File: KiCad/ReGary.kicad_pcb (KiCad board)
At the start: 4 copper layers, 38 x 38 mm, 38 parts, among them J1 Conn_01x02, U1 GW1N-UV1P5LQ100, U2 LM1117-3.3, U3 TPS73643DBV, U4 SN74CBT16210, U5 SN74CBT16210, U6 SN74CBT16210, U7 SN74CBT16210, U8 PLCC_84_plug, U9 PLCC_84_plug

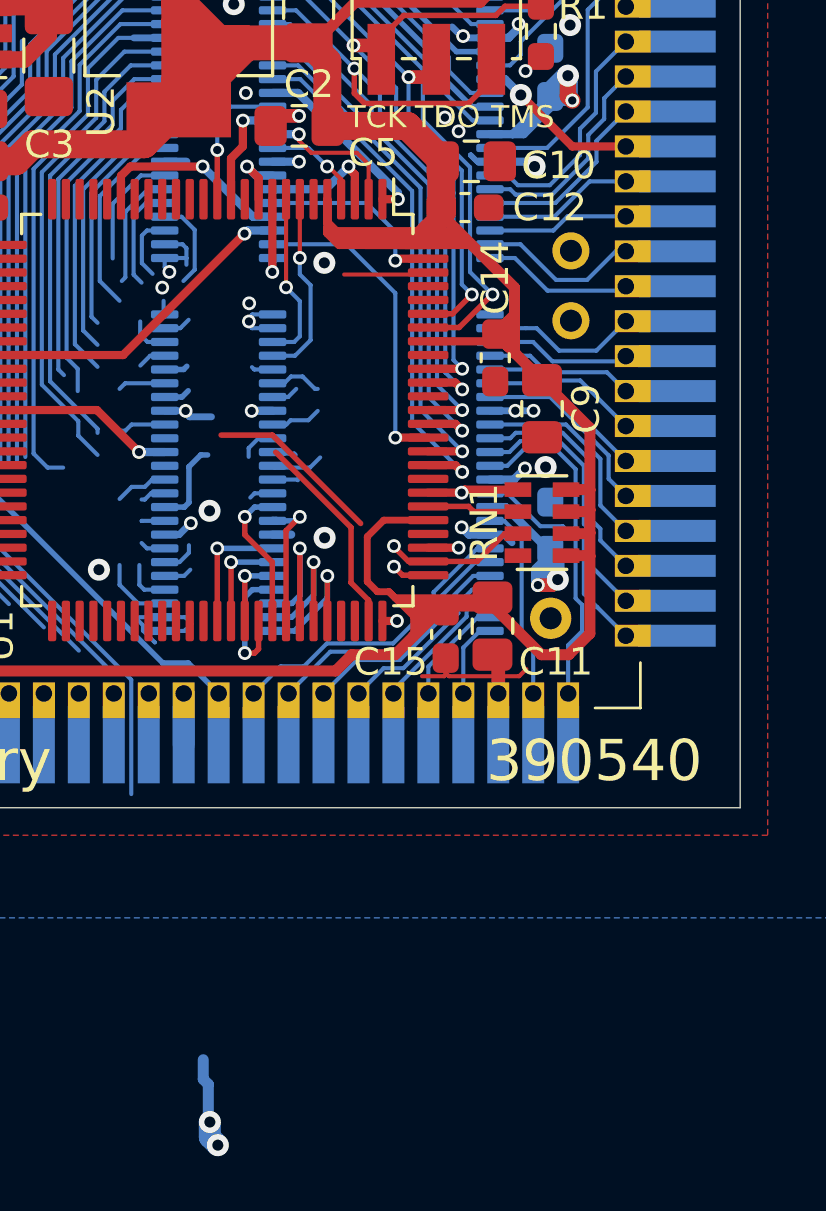
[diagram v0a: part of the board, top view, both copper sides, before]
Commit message: More signal to pin assignments and routing done, moved /REGEN and /RAMEN signals to FPGA pin 97,98
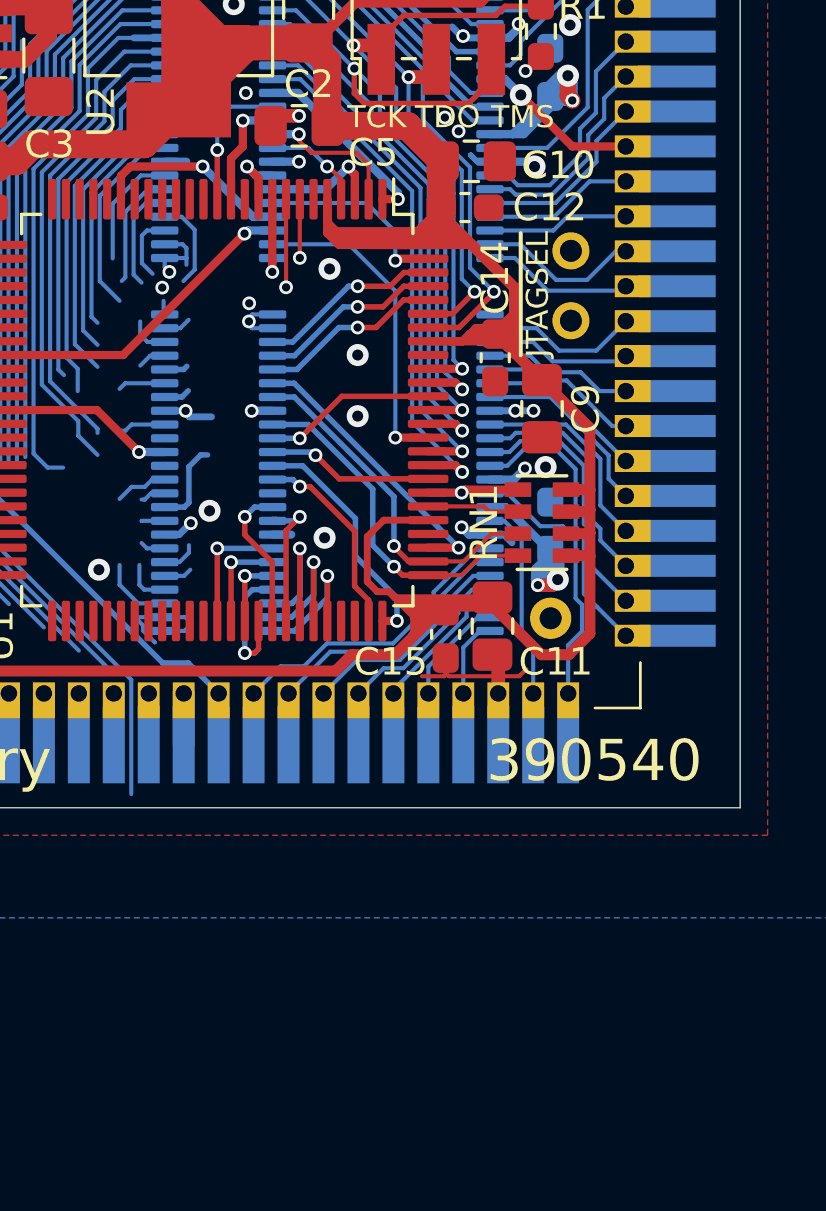
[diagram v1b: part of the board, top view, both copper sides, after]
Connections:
- U1 pad 7: REGEN_FPGA -> Net-(U1-Pad7)
- U1 pad 8: RAMEN_FPGA -> Net-(U1-Pad8)
- U1 pad 83: Net-(U1-Pad83) -> PWRUP_FPGA
- U1 pad 89: Net-(U1-Pad89) -> A12_FPGA
- U1 pad 96: Net-(U1-Pad96) -> BLS_FPGA
- U1 pad 97: Net-(U1-Pad97) -> REGEN_FPGA
- U1 pad 98: Net-(U1-Pad98) -> RAMEN_FPGA
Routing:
- net UDS_FPGA: track 3.22 -> 12.7 mm
- net DBR_FPGA: track 3.04 -> 10.3 mm
- net LDS_FPGA: track 6.16 -> 12.9 mm
- net BLS_FPGA: track 0.79 -> 6.70 mm, vias 0 -> 1
- net PWRUP_FPGA: track 0.88 -> 6.06 mm, vias 0 -> 1
- net A12_FPGA: track 1.34 -> 6.28 mm, vias 0 -> 1
- net Net-(U1-Pad8): track 0.00 -> 3.20 mm, vias 0 -> 1
- net Net-(U1-Pad98): track 3.08 -> 0.00 mm
- net Net-(U1-Pad7): track 0.00 -> 2.13 mm, vias 0 -> 1
- net OECD_FPGA: track 8.46 -> 7.23 mm, vias 0 -> 1
- net Net-(U6-Pad35): track 0.87 -> 0.00 mm
- net 3V3: track 156.4 -> 156.3 mm, vias 2 -> 0
- net GND: vias 37 -> 39
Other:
- board text added: "~JTAGSEL"

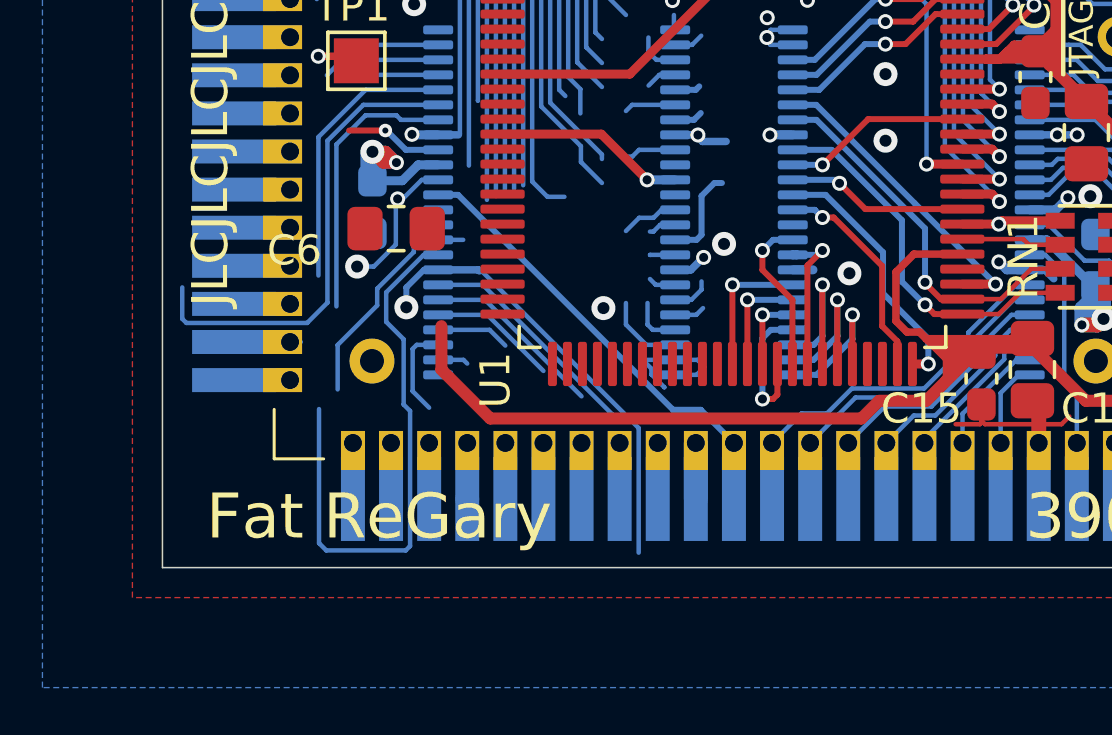
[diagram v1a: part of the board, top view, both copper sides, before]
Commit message: More pin assignments and routing
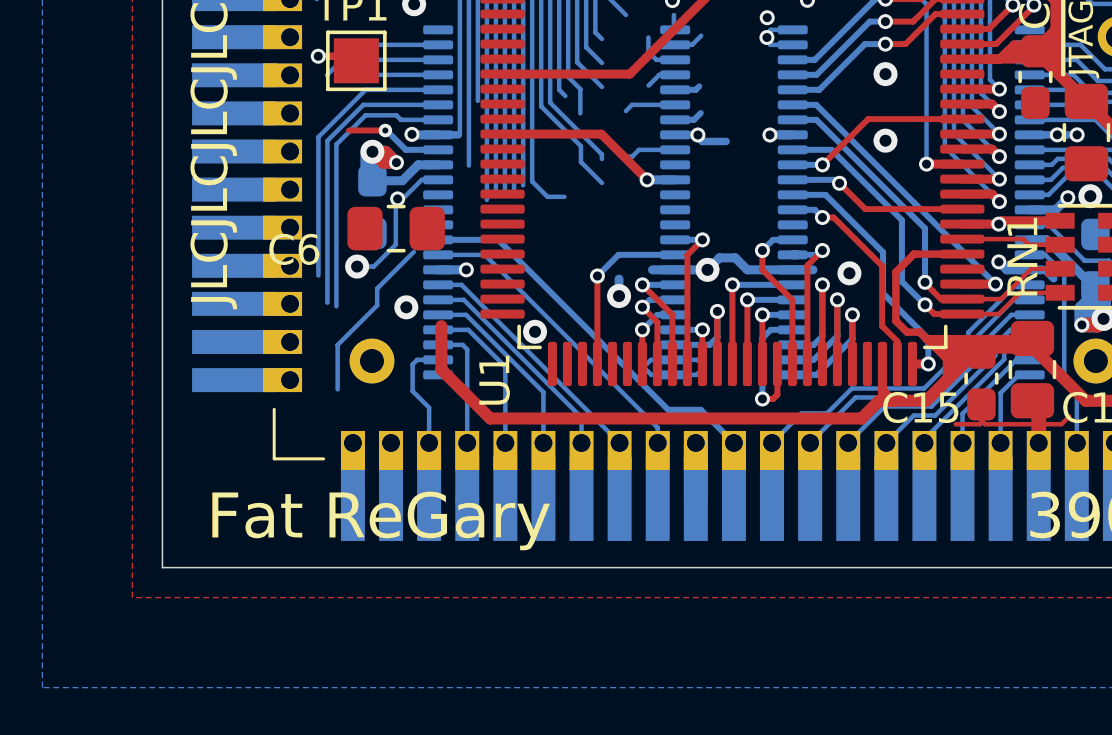
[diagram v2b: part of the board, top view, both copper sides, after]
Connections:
- net ABOE2 renamed Net-(U7-Pad11)
- net ABOE2_FPGA renamed Net-(U7-Pad37)
- net DBOE1 renamed Net-(U7-Pad12)
- net DBOE1_FPGA renamed Net-(U7-Pad36)
- net HLT renamed Net-(U7-Pad21)
- net HLT_FPGA renamed Net-(U7-Pad28)
- U1 pad 54: Net-(U1-Pad54) -> BERR_FPGA
- U1 pad 57: Net-(U1-Pad57) -> ROMJP0_FPGA
- U1 pad 58: Net-(U1-Pad58) -> ROMJP1_FPGA
- U1 pad 59: Net-(U1-Pad59) -> AVEC_FPGA
- U1 pad 60: Net-(U1-Pad60) -> CIIN_FPGA
- U1 pad 61: Net-(U1-Pad61) -> RESET_FPGA
- U1 pad 62: Net-(U1-Pad62) -> A15_FPGA
- U5 pad 42: CIIN_FPGA -> Net-(U5-Pad42)
- U5 pad 6: CIIN -> Net-(U5-Pad6)
- U7 pad 10: LOCK_EA1 -> CPUCLK
- U7 pad 13: CPUCLK -> Net-(U7-Pad13)
- U7 pad 14: GND -> Net-(U7-Pad14)
- U7 pad 16: BERR -> Net-(U7-Pad16)
- U7 pad 18: C7M -> Net-(U7-Pad18)
- U7 pad 19: RESET -> Net-(U7-Pad19)
- U7 pad 2: DBR16 -> A15
- U7 pad 20: CPUCLK -> Net-(U7-Pad20)
- U7 pad 3: DBOE0 -> RESET
- U7 pad 30: RESET_FPGA -> Net-(U7-Pad30)
- U7 pad 31: C7M_FPGA -> Net-(U7-Pad31)
- U7 pad 33: BERR_FPGA -> Net-(U7-Pad33)
- U7 pad 35: CPUCLK_FPGA -> Net-(U7-Pad35)
- U7 pad 38: LOCK_EA1_FPGA -> CPUCLK_FPGA
- U7 pad 39: CDAC_FPGA -> CIIN_FPGA
- U7 pad 4: DBLT -> ROMJP0
- U7 pad 40: EDS3_FPGA -> BERR_FPGA
- U7 pad 42: EDS2_FPGA -> AVEC_FPGA
- U7 pad 43: READ_FPGA -> ROMJP1_FPGA
- U7 pad 44: DBLT_FPGA -> ROMJP0_FPGA
- U7 pad 45: DBOE0_FPGA -> RESET_FPGA
- U7 pad 46: DBR16_FPGA -> A15_FPGA
- U7 pad 5: READ -> ROMJP1
- U7 pad 6: EDS2 -> AVEC
- U7 pad 7: EDS3 -> BERR
- U7 pad 9: CDAC -> CIIN
- U8 pad 35: Net-(U8-Pad35) -> A15
- U8 pad 36: Net-(U8-Pad36) -> RESET
- U8 pad 37: Net-(U8-Pad37) -> ROMJP0
- U8 pad 38: Net-(U8-Pad38) -> ROMJP1
- U8 pad 39: Net-(U8-Pad39) -> AVEC
- U8 pad 40: Net-(U8-Pad40) -> BERR
- U8 pad 41: Net-(U8-Pad41) -> CIIN
- U9 pad 35: Net-(U9-Pad35) -> A15
- U9 pad 36: Net-(U9-Pad36) -> RESET
- U9 pad 37: Net-(U9-Pad37) -> ROMJP0
- U9 pad 38: Net-(U9-Pad38) -> ROMJP1
- U9 pad 39: Net-(U9-Pad39) -> AVEC
- U9 pad 40: Net-(U9-Pad40) -> BERR
- U9 pad 41: Net-(U9-Pad41) -> CIIN
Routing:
- net CDAC: track 23.9 -> 5.15 mm
- net GND: track 103.4 -> 87.2 mm, vias 39 -> 38
- net RESET: track 15.8 -> 4.15 mm
- net CIIN: track 4.56 -> 15.8 mm
- net CPUCLK: track 22.5 -> 12.7 mm
- net Net-(U7-Pad19): track 0.00 -> 9.58 mm
- net Net-(U7-Pad20): track 0.00 -> 9.26 mm
- net C7M: track 14.7 -> 5.47 mm
- net Net-(U7-Pad18): track 0.00 -> 9.25 mm
- net Net-(TP1-Pad1): track 16.5 -> 8.27 mm
- net EDS3: track 7.94 -> 0.00 mm
- net Net-(U7-Pad12): track 7.67 -> 0.00 mm
- net AVEC: track 0.00 -> 7.25 mm
- net ROMJP1: track 0.00 -> 6.27 mm
- net EDS2: track 6.11 -> 0.00 mm
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
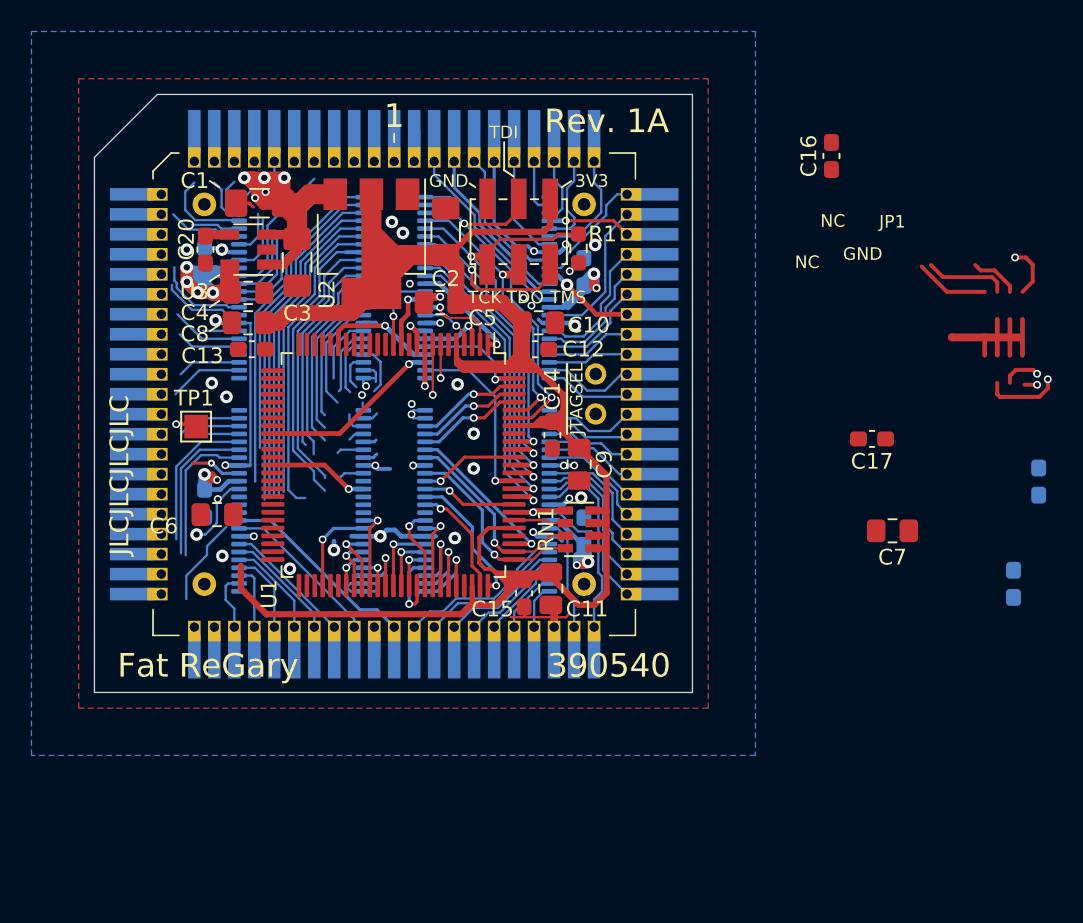
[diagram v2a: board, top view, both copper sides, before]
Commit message: Placement of caps and more routing of 3V3-power
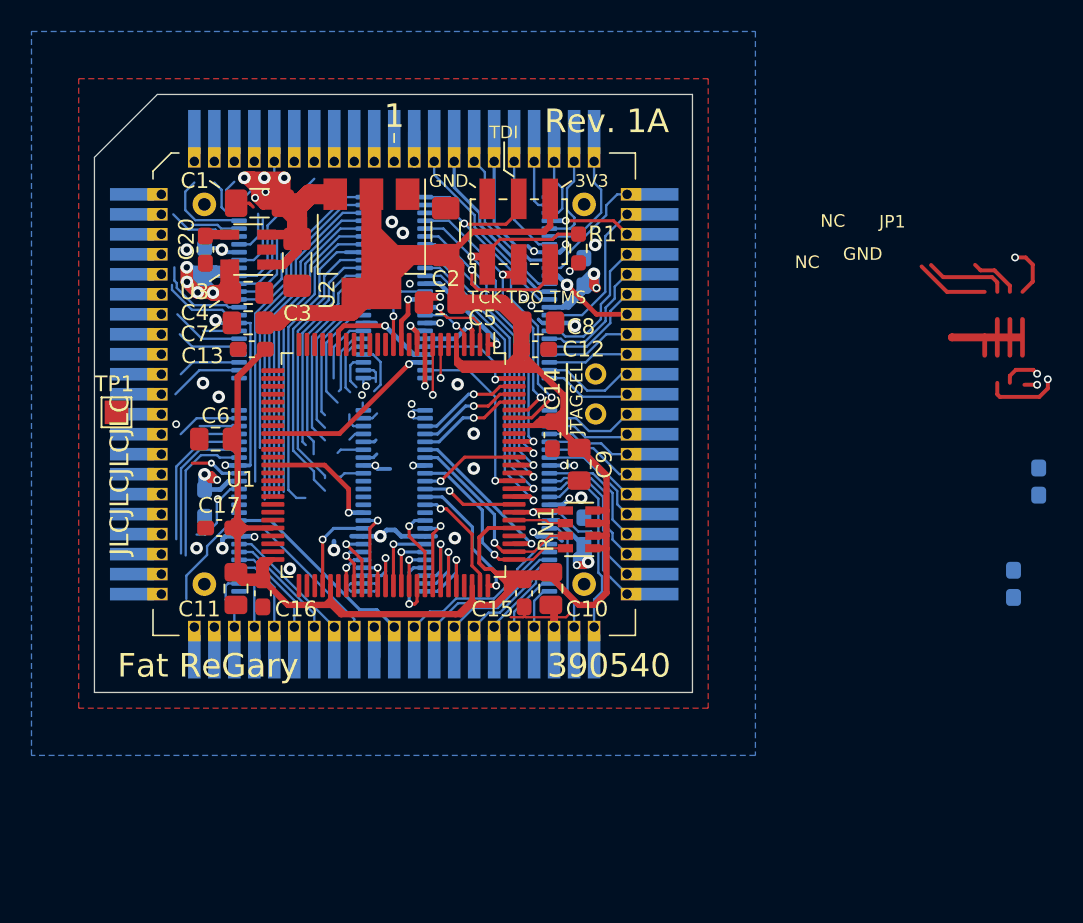
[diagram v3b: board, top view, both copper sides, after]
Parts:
- C11: renamed from C7; value 1uF -> 0.1uF
- moved C16 45.6 mm to (136.1, 87.1)
- moved C11 41.9 mm to (134.4, 86.8), turned to 90 degrees
- moved C17 41.9 mm to (133.3, 83.0), turned to 0 degrees
- moved TP1 5.14 mm to (126.8, 75.6)
- moved C6 4.80 mm to (133.1, 77.3)
- renumbered C11 to C10, C8 to C7, C10 to C8
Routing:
- net 3V3: track 158.9 -> 197.1 mm
- net GND: track 87.2 -> 88.9 mm
- net CPUCLK_FPGA: track 6.38 -> 7.88 mm
- net Net-(TP1-Pad1): track 8.27 -> 6.93 mm

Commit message: More pin assignments and routing
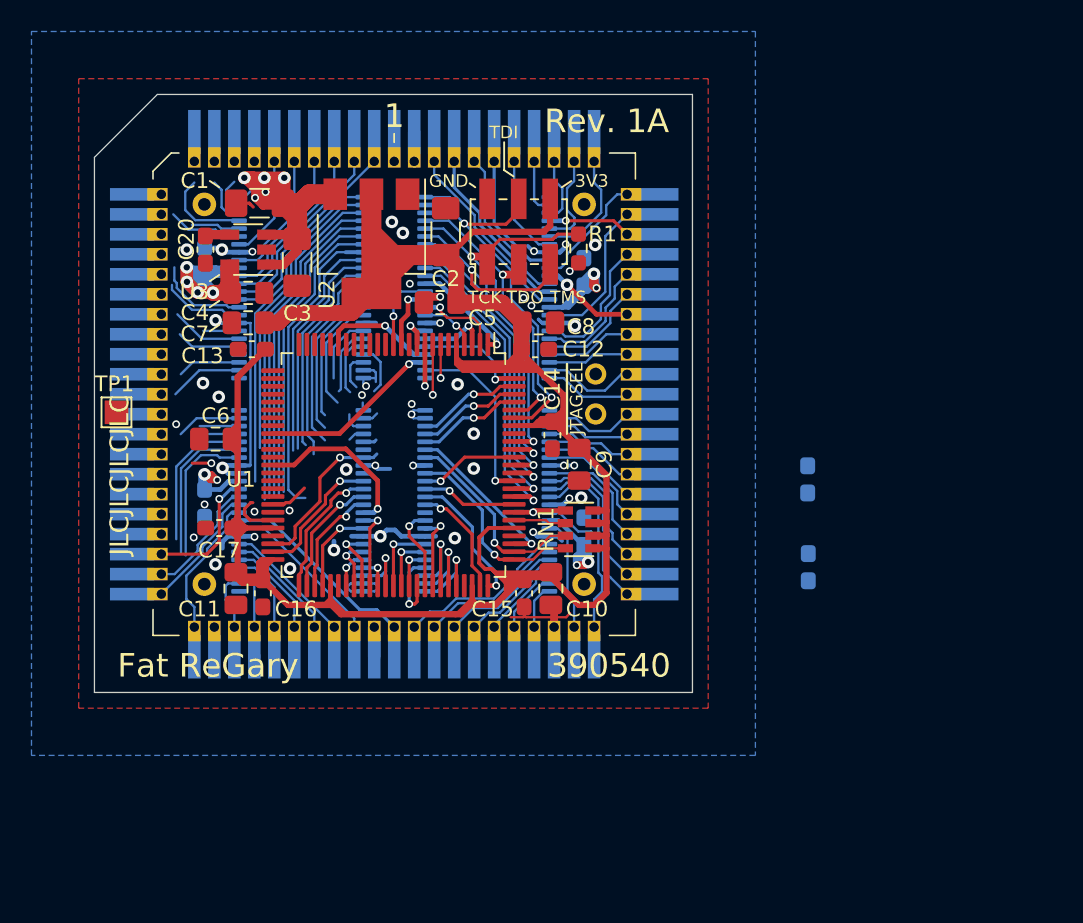
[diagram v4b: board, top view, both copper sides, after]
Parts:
- moved C19 14.7 mm to (170.7, 79.9)
- moved C18 13.1 mm to (170.8, 85.4)
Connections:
- net A0_FPGA renamed A28_FPGA
- net A1_FPGA renamed A29_FPGA
- net A2_FPGA renamed A30_FPGA
- net AS renamed Net-(U5-Pad23)
- net AS_FPGA renamed Net-(U5-Pad26)
- net BG renamed Net-(U7-Pad23)
- net BGACK renamed Net-(U7-Pad22)
- net BGACK_FPGA renamed Net-(U7-Pad27)
- net BG_FPGA renamed Net-(U7-Pad26)
- net BR renamed Net-(U7-Pad24)
- net BR_FPGA renamed Net-(U7-Pad25)
- net CCS_FPGA renamed A31_FPGA
- net DOE renamed Net-(U5-Pad3)
- net DOE_FPGA renamed Net-(U5-Pad45)
- net DTACK renamed Net-(U5-Pad4)
- net DTACK_FPGA renamed Net-(U5-Pad44)
- net MTACK renamed Net-(U5-Pad5)
- net MTACK_FPGA renamed Net-(U5-Pad43)
- net RMC renamed Net-(U5-Pad10)
- net RMC_FPGA renamed Net-(U5-Pad38)
- net RW_FPGA renamed A27_FPGA
- net SBG renamed Net-(U5-Pad7)
- net SBG_FPGA renamed Net-(U5-Pad40)
- net SBR renamed Net-(U5-Pad9)
- net SBR_FPGA renamed Net-(U5-Pad39)
- net WAIT renamed Net-(U5-Pad2)
- net WAIT_FPGA renamed Net-(U5-Pad46)
- U1 pad 48: Net-(U1-Pad48) -> DSACK0_FPGA
- U1 pad 49: Net-(U1-Pad49) -> DSACK1_FPGA
- U1 pad 51: Net-(U1-Pad51) -> A13_FPGA
- U1 pad 52: Net-(U1-Pad52) -> A14_FPGA
- U1 pad 53: Net-(U1-Pad53) -> OVL_FPGA
- U5 pad 11: CCS -> A31
- U5 pad 12: A2 -> A30
- U5 pad 13: A1 -> A29
- U5 pad 14: A0 -> A28
- U5 pad 16: RW -> A27
- U5 pad 18: SIZ0 -> A26
- U5 pad 19: STERM -> IENA
- U5 pad 20: DSACK1 -> A25
- U5 pad 21: DSACK0 -> A24
- U5 pad 22: DS -> Net-(U5-Pad22)
- U5 pad 24: SIZ1 -> Net-(U5-Pad24)
- U5 pad 25: SIZ1_FPGA -> Net-(U5-Pad25)
- U5 pad 27: DS_FPGA -> Net-(U5-Pad27)
- U5 pad 28: DSACK0_FPGA -> A24_FPGA
- U5 pad 29: DSACK1_FPGA -> A25_FPGA
- U5 pad 30: STERM_FPGA -> IENA_FPGA
- U5 pad 31: SIZ0_FPGA -> A26_FPGA
- U7 pad 11: Net-(U7-Pad11) -> OVL
- U7 pad 12: Net-(U7-Pad12) -> A14
- U7 pad 13: Net-(U7-Pad13) -> A13
- U7 pad 14: Net-(U7-Pad14) -> DSACK1
- U7 pad 16: Net-(U7-Pad16) -> GND
- U7 pad 18: Net-(U7-Pad18) -> DSACK0
- U7 pad 19: Net-(U7-Pad19) -> SIZ1
- U7 pad 20: Net-(U7-Pad20) -> SIZ0
- U7 pad 29: Net-(U7-Pad29) -> SIZ0_FPGA
- U7 pad 30: Net-(U7-Pad30) -> SIZ1_FPGA
- U7 pad 31: Net-(U7-Pad31) -> DSACK0_FPGA
- U7 pad 34: Net-(U7-Pad34) -> DSACK1_FPGA
- U7 pad 35: Net-(U7-Pad35) -> A13_FPGA
- U7 pad 36: Net-(U7-Pad36) -> A14_FPGA
- U7 pad 37: Net-(U7-Pad37) -> OVL_FPGA
- U8 pad 10: Net-(U8-Pad10) -> A24
- U8 pad 2: Net-(U8-Pad2) -> A31
- U8 pad 27: Net-(U8-Pad27) -> SIZ0
- U8 pad 28: Net-(U8-Pad28) -> SIZ1
- U8 pad 29: Net-(U8-Pad29) -> DSACK0
- U8 pad 3: Net-(U8-Pad3) -> A30
- U8 pad 30: Net-(U8-Pad30) -> DSACK1
- U8 pad 31: Net-(U8-Pad31) -> A13
- U8 pad 32: Net-(U8-Pad32) -> A14
- U8 pad 33: Net-(U8-Pad33) -> OVL
- U8 pad 4: Net-(U8-Pad4) -> A29
- U8 pad 5: Net-(U8-Pad5) -> A28
- U8 pad 6: Net-(U8-Pad6) -> A27
- U8 pad 7: Net-(U8-Pad7) -> A26
- U8 pad 8: Net-(U8-Pad8) -> IENA
- U8 pad 9: Net-(U8-Pad9) -> A25
- U9 pad 10: Net-(U9-Pad10) -> A24
- U9 pad 2: Net-(U9-Pad2) -> A31
- U9 pad 27: Net-(U9-Pad27) -> SIZ0
- U9 pad 28: Net-(U9-Pad28) -> SIZ1
- U9 pad 29: Net-(U9-Pad29) -> DSACK0
- U9 pad 3: Net-(U9-Pad3) -> A30
- U9 pad 30: Net-(U9-Pad30) -> DSACK1
- U9 pad 31: Net-(U9-Pad31) -> A13
- U9 pad 32: Net-(U9-Pad32) -> A14
- U9 pad 33: Net-(U9-Pad33) -> OVL
- U9 pad 4: Net-(U9-Pad4) -> A29
- U9 pad 5: Net-(U9-Pad5) -> A28
- U9 pad 6: Net-(U9-Pad6) -> A27
- U9 pad 7: Net-(U9-Pad7) -> A26
- U9 pad 8: Net-(U9-Pad8) -> IENA
- U9 pad 9: Net-(U9-Pad9) -> A25
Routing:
- net SIZ1_FPGA: track 21.6 -> 0.00 mm
- net Net-(U5-Pad25): track 0.00 -> 21.6 mm
- net Net-(U5-Pad27): track 0.00 -> 21.6 mm
- net DS_FPGA: track 40.6 -> 19.1 mm
- net A24_FPGA: track 0.00 -> 20.9 mm
- net A25_FPGA: track 0.00 -> 20.2 mm
- net STERM_FPGA: track 23.2 -> 3.69 mm
- net IENA_FPGA: track 0.00 -> 19.5 mm
- net A26_FPGA: track 0.00 -> 18.8 mm
- net SIZ0_FPGA: track 18.8 -> 0.85 mm
- net A31: track 0.00 -> 13.2 mm
- net 3V3: track 197.1 -> 184.8 mm
- net A30: track 0.00 -> 12.1 mm
- net DSACK1_FPGA: track 20.2 -> 8.44 mm, vias 0 -> 1
- net A29: track 0.00 -> 11.0 mm
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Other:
- board text removed: "JP1"
- board text removed: "NC"
